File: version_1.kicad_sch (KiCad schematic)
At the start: 17 parts, among them U1 Pico, U10 74AHC595, U12 LSM6DS3

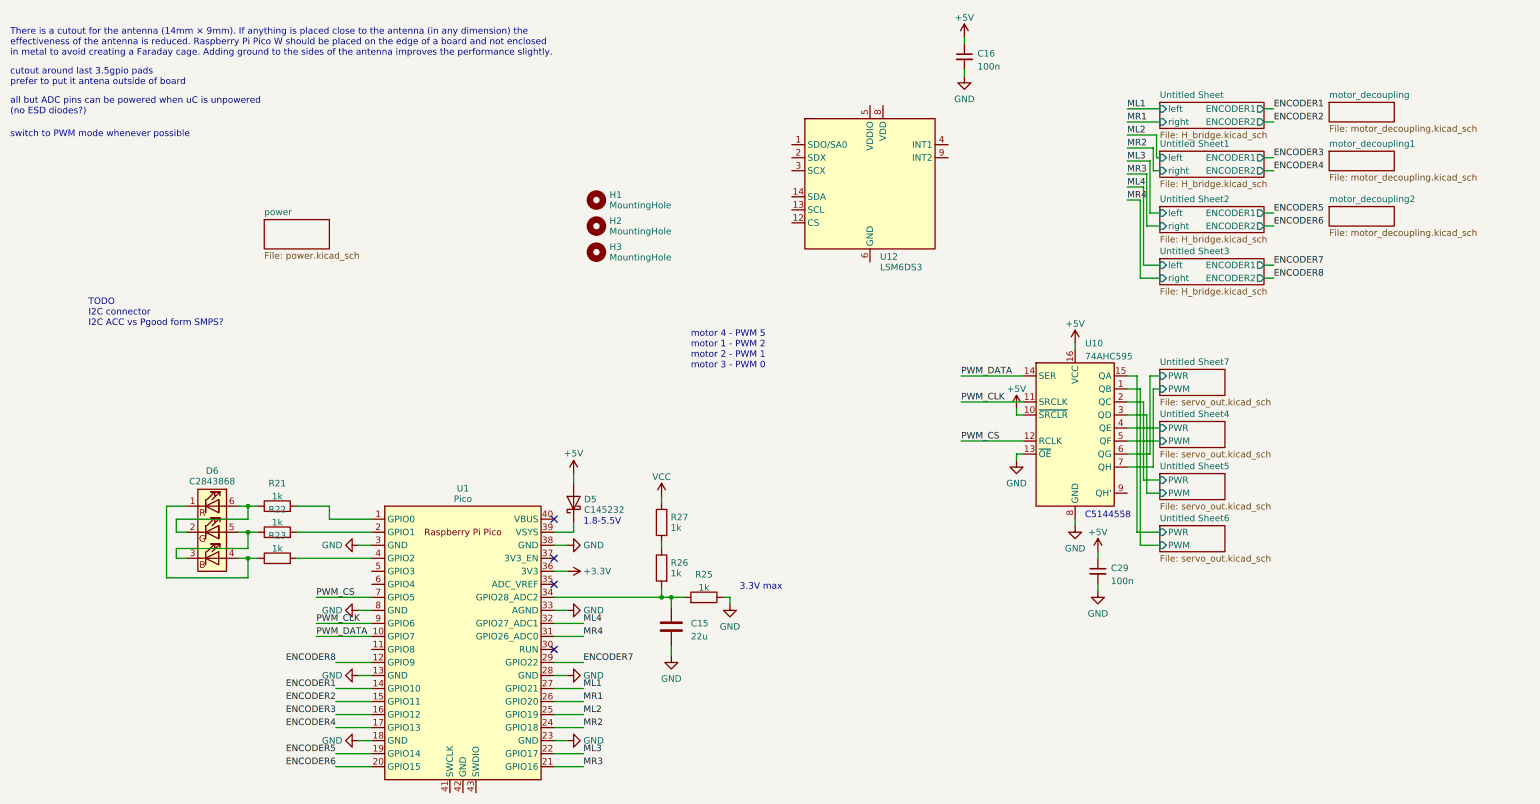
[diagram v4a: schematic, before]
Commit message: version 1.1 item colisions fixed added silkscreen DRC done
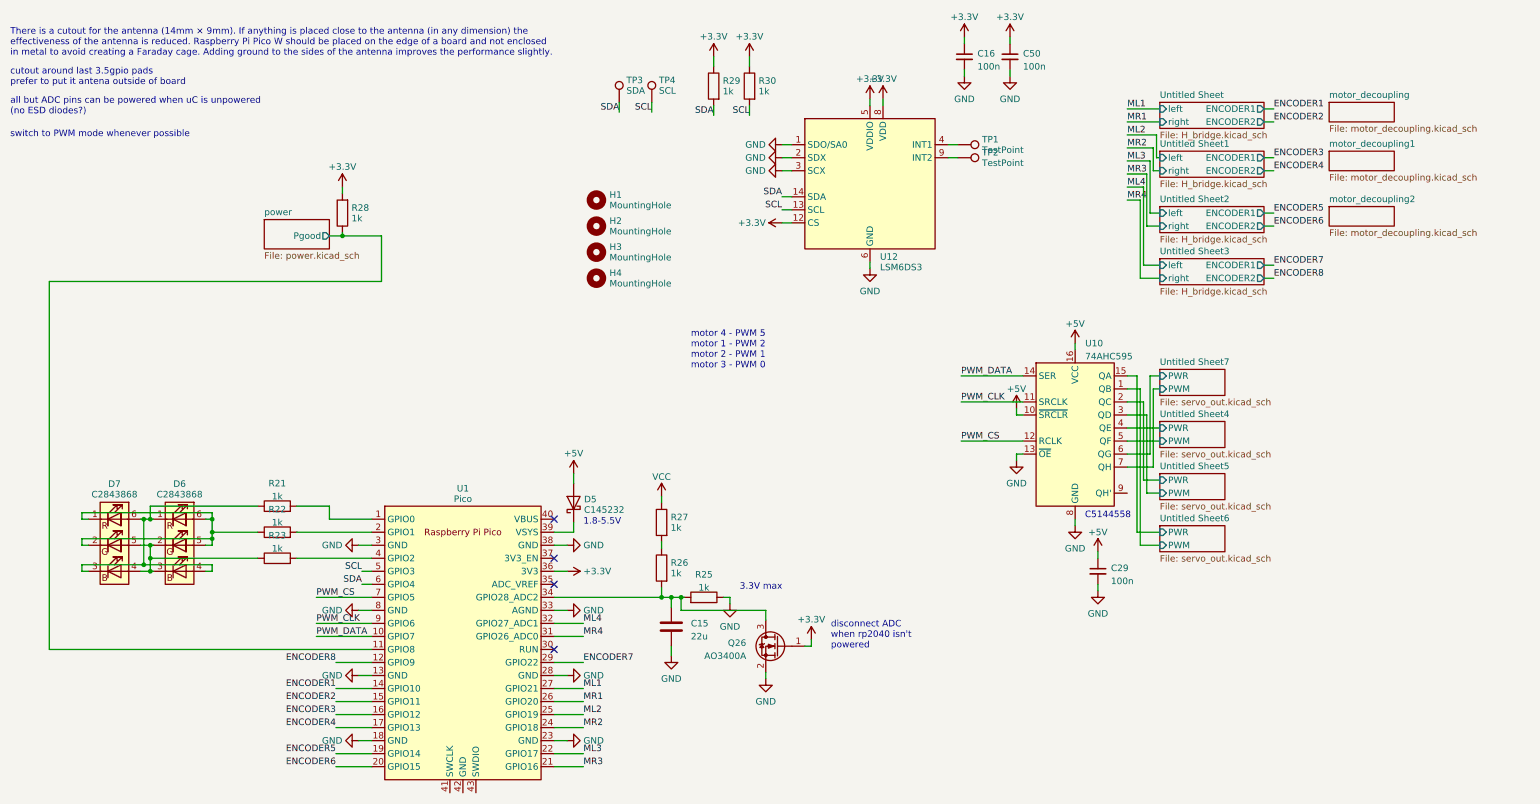
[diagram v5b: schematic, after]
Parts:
- added C50: 100n, Capacitor_SMD:C_0603_1608Metric_Pad1.08x0.95mm_HandSolder, symbol Device:C_Small
- added D7: C2843868, LED_SMD:LED_RGB_5050-6, symbol Device:LED_RGB
- added H4: MountingHole, MountingHole:MountingHole_3.2mm_M3, symbol Mechanical:MountingHole
- added Q26: AO3400A, Package_TO_SOT_SMD:SOT-23, symbol Transistor_FET:AO3400A
- added R28, R29, R30: 1k, Resistor_SMD:R_0603_1608Metric_Pad0.98x0.95mm_HandSolder, symbol Device:R
- added TP1, TP2: TestPoint, TestPoint:TestPoint_Pad_D2.0mm, symbol Connector:TestPoint
- added TP3: SDA, TestPoint:TestPoint_Pad_D2.0mm, symbol Connector:TestPoint
- added TP4: SCL, TestPoint:TestPoint_Pad_D2.0mm, symbol Connector:TestPoint
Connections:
- net +3.3V: now also C16.1, U12.12 (CS), U12.5 (VDDIO), U12.8 (VDD), C50.1, Q26.1 (G), R28.2, R29.1, R30.1
- net +5V: no longer C16.1
- net GND: now also U12.1 (SDO/SA0), U12.2 (SDX), U12.3 (SCX), U12.6 (GND), U12.7 (GND), C50.2, Q26.2 (S)
- net at D6.1 (RK), D6.4 (BA): now also R21.1, D7.3 (BK), D7.6 (RA); no longer R23.1
- net at D6.5 (GA), R22.1: now also D6.6 (RA), D7.1 (RK), D7.2 (GK); no longer D6.3 (BK)
- net at C15.1, R25.2, R26.2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: now also Q26.3 (D)
- net SCL: now reaches U12.13 (SCL)
- net SCL: now also U1.5 (GPIO3), R30.2, TP4.1
- net SDA: now reaches U12.14 (SDA)
- net SDA: now also U1.6 (GPIO4), R29.2, TP3.1
- net at U12.4 (INT1): now also TP1.1
- net at U12.9 (INT2): now also TP2.1
- net power/Pgood: now reaches U1.11 (GPIO8)
- net power/Pgood: now also R28.1
- new net: D6.2 (GK), D6.3 (BK), D7.4 (BA), D7.5 (GA), R23.1
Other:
- sheet power ports: added Pgood; removed none
- note added: "disconnect ADC when rp2040 isn't powered"
- note removed: "TODO I2C connector I2C ACC vs Pgood form SMPS?"
- moved on the sheet: D6

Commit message: new version of layout with diodes improved power routing a little bit
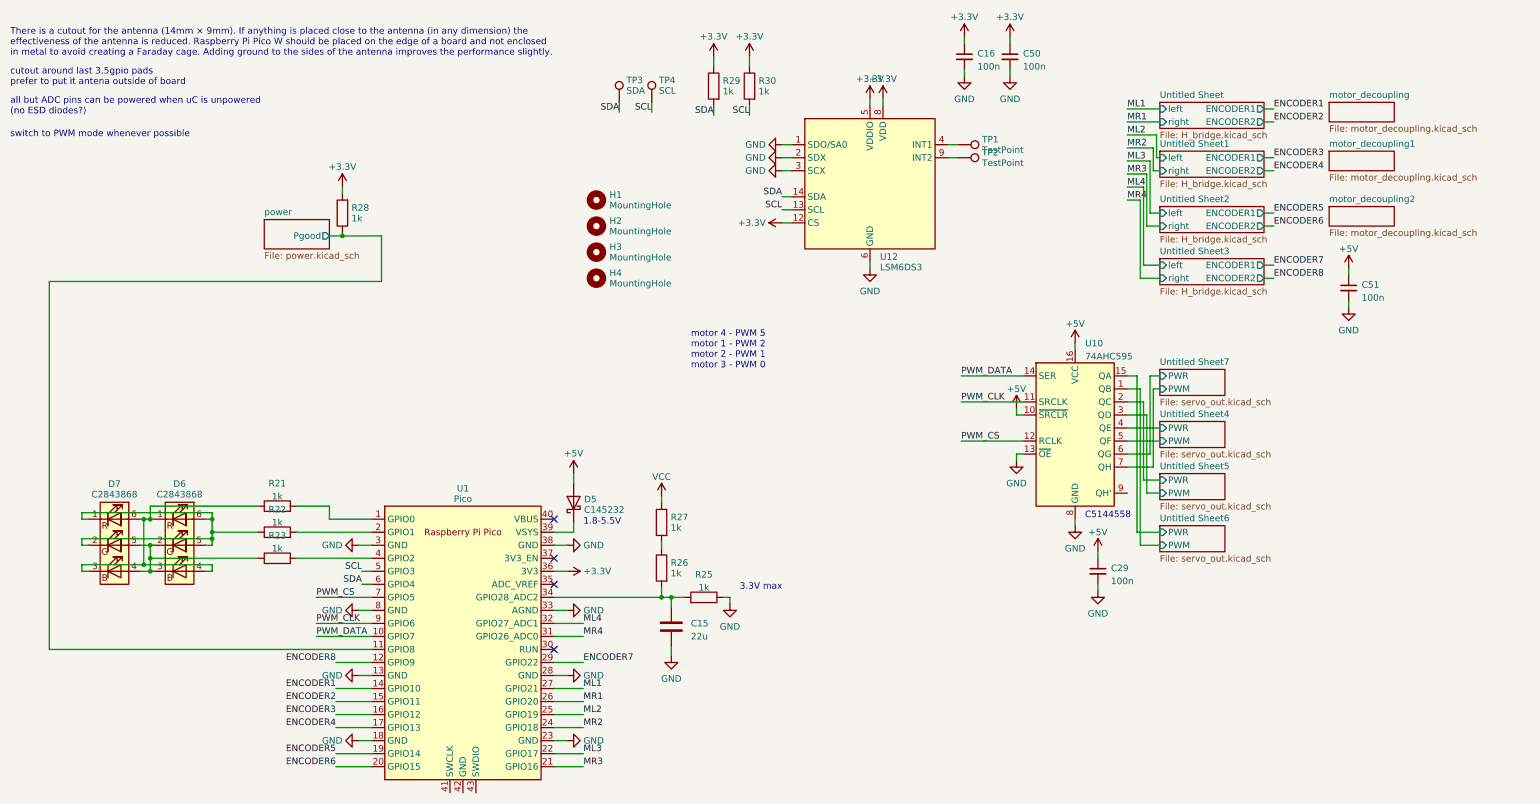
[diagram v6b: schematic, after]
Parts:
- removed Q26: AO3400A, Package_TO_SOT_SMD:SOT-23, symbol Transistor_FET:AO3400A
- added C51: 100n, Capacitor_SMD:C_0603_1608Metric_Pad1.08x0.95mm_HandSolder, symbol Device:C_Small
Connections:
- net +5V: now also C51.1
- net GND: now also C51.2
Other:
- note removed: "disconnect ADC when rp2040 isn't powered"

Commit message: najnowsza wersja
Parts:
- removed D7: C2843868, LED_SMD:LED_RGB_5050-6, symbol Device:LED_RGB
- U12: value LSM6DS3 -> C967633
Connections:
- net GND: now also D6.1 (RK), D6.2 (GK), D6.3 (BK)
- net SDA: now also U1.4 (GPIO2); no longer U1.6 (GPIO4)
- net at D6.5 (GA), R22.1: no longer D6.6 (RA)
- net at R23.2: now also U1.6 (GPIO4); no longer U1.4 (GPIO2)
- new net: D6.4 (BA), R23.1
- new net: D6.6 (RA), R21.1
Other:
- moved on the sheet: D6

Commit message: jlcpcb part numbs
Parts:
- D5: JLCPCB Part# (none) -> C145232
- D6: JLCPCB Part# (none) -> C2843868
- U1: JLCPCB Part # (none) -> C7203003
- U10: JLCPCB Part# (none) -> C2682116
- U12: JLCPCB Part# (none) -> C967633
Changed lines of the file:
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@@
     )
     (property "Value" "C2843868" (at 52.705 105.021 0)
-      (effects (font (size 1.27 1.27)))
+      (effects (font (size 1.27 1.27)) hide)
     )
     (property "Footprint" "LED_SMD:LED_RGB_5050-6" (at 52.705 116.205 0)
@@
     )
     (property "Datasheet" "~" (at 52.705 116.205 0)
+      (effects (font (size 1.27 1.27)) hide)
+    )
+    (property "JLCPCB Part#" "C2843868" (at 52.705 114.935 0)
       (effects (font (size 1.27 1.27)) hide)
     )
@@
       (effects (font (size 1.27 1.27)) hide)
     )
+    (property "JLCPCB Part#" "C145232" (at 128.27 109.22 90)
+      (effects (font (size 1.27 1.27)) hide)
+    )
     (pin "1")
     (pin "2")
@@
     )
     (property "Datasheet" "https://www.st.com/resource/en/datasheet/lsm6ds3tr-c.pdf" (at 188.595 63.5 0)
+      (effects (font (size 1.27 1.27)) hide)
+    )
+    (property "JLCPCB Part#" "C967633" (at 186.055 46.99 0)
       (effects (font (size 1.27 1.27)) hide)
     )
@@
     )
     (property "Datasheet" "" (at 106.68 136.525 0)
+      (effects (font (size 1.27 1.27)) hide)
+    )
+    (property "JLCPCB Part #" "C7203003" (at 106.68 136.525 0)
       (effects (font (size 1.27 1.27)) hide)
     )
@@
       (effects (font (size 1.27 1.27)) hide)
     )
+    (property "JLCPCB Part#" "C2682116" (at 226.06 94.615 0)
+      (effects (font (size 1.27 1.27)) hide)
+    )
